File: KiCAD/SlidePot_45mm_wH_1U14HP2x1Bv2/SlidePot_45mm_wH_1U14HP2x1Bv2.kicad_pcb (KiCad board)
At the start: 2 copper layers, 70.8 x 39.7 mm, 7 parts

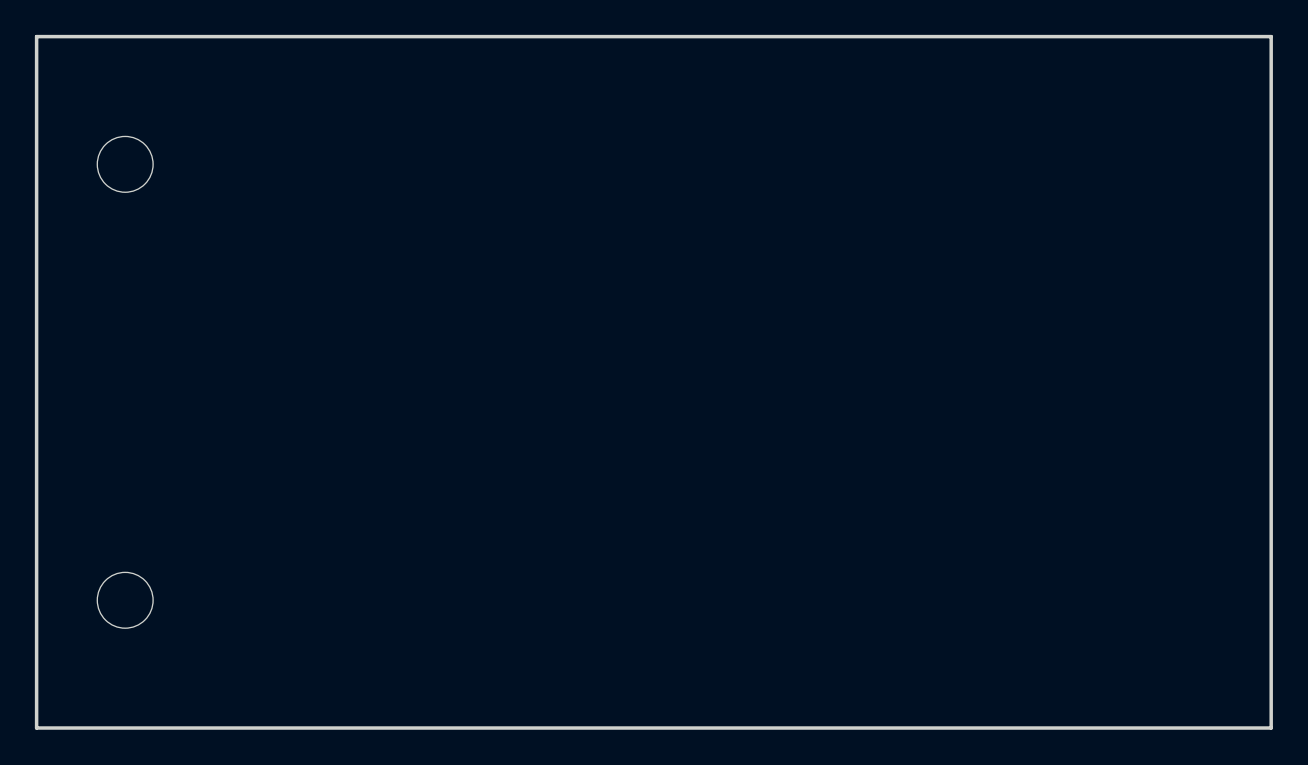
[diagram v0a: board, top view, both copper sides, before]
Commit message: updated all modules to use plated through-holes wherever possible
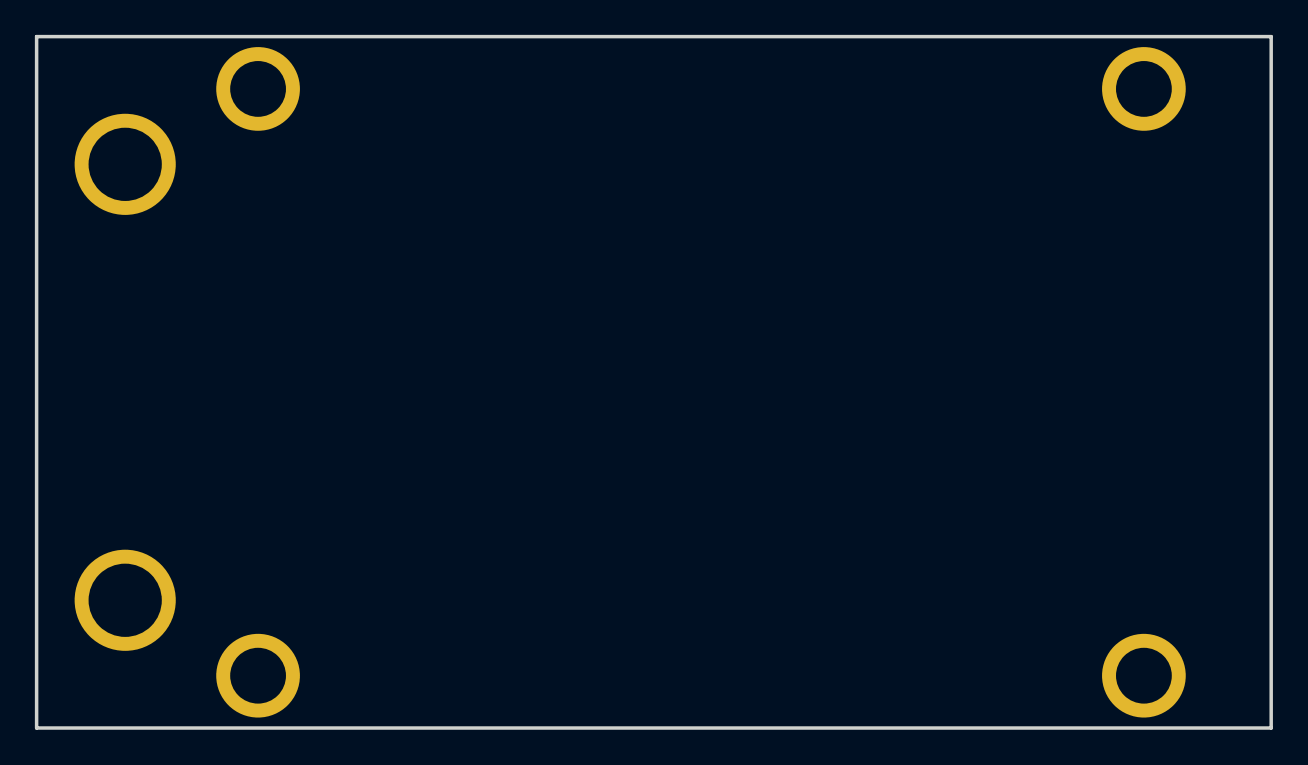
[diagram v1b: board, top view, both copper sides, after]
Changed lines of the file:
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@@
 			)
 		)
-		(pad "" np_thru_hole oval
+		(pad "" thru_hole circle
 			(at 0 0)
-			(size 4.34 3.2)
-			(drill oval 4.34 3.2)
+			(size 4.8 4.8)
+			(drill 3.2)
 			(layers "*.Cu" "*.Mask")
+			(remove_unused_layers no)
 		)
 		(embedded_fonts no)
@@
 			)
 		)
-		(pad "" np_thru_hole oval
+		(pad "" thru_hole circle
 			(at 0 0)
-			(size 4.34 3.2)
-			(drill oval 4.34 3.2)
+			(size 4.8 4.8)
+			(drill 3.2)
 			(layers "*.Cu" "*.Mask")
+			(remove_unused_layers no)
 		)
 		(embedded_fonts no)
@@
 			)
 		)
-		(pad "" np_thru_hole circle
+		(pad "" thru_hole circle
 			(at 0 0)
-			(size 3.2 3.2)
-			(drill 3.2)
+			(size 5.8 5.8)
+			(drill 4.2)
 			(layers "*.Cu" "*.Mask")
-		)
-		(pad "" np_thru_hole circle
+			(remove_unused_layers no)
+		)
+		(pad "" thru_hole circle
 			(at 0 25)
-			(size 3.2 3.2)
-			(drill 3.2)
+			(size 5.8 5.8)
+			(drill 4.2)
 			(layers "*.Cu" "*.Mask")
+			(remove_unused_layers no)
 		)
 		(embedded_fonts no)
@@
 			)
 		)
-		(pad "" np_thru_hole oval
+		(pad "" thru_hole circle
 			(at 0 0)
-			(size 4.34 3.2)
-			(drill oval 4.34 3.2)
+			(size 4.8 4.8)
+			(drill 3.2)
 			(layers "*.Cu" "*.Mask")
+			(remove_unused_layers no)
 		)
 		(embedded_fonts no)
@@
 			)
 		)
-		(pad "" np_thru_hole oval
+		(pad "" thru_hole circle
 			(at 0 0)
-			(size 4.34 3.2)
-			(drill oval 4.34 3.2)
+			(size 4.8 4.8)
+			(drill 3.2)
 			(layers "*.Cu" "*.Mask")
+			(remove_unused_layers no)
 		)
 		(embedded_fonts no)
